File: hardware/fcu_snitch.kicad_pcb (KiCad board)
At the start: 2 copper layers, 105 parts, among them IC1 STM32WLE5CCU6, J1 SMA, J2 02x03_JST_SWD, J3 Conn_02x04_Top_Bottom, J4 Conn_01x02_Socket, J5 Conn_01x04_Socket, Q1 NPN, U1 SKY13373-460LF, U2 BALFHB-WL-02D3, U3 SN74LVC1G3157DBVR, U4 LPS22HBTR, U5 LSM6DSO32, Y1 ABS07L-32.768KHZ-T, Y2 ASTX-H11

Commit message: schematic update and pcb route v1
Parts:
- removed C16: 100p, Capacitor_SMD:C_0402_1005Metric
- removed C47: 100n, Capacitor_SMD:C_0805_2012Metric
- removed C48, C49: 6.8p, Capacitor_SMD:C_0805_2012Metric
- added BT1: Battery_Cell, Battery:BatteryHolder_Keystone_3034_1x20mm, B.Cu at (133.7, 106.5)
- added C8: 100n, Capacitor_SMD:C_0805_2012Metric, B.Cu at (108.8, 97.9)
- added C9: 4.7u, Capacitor_SMD:C_0805_2012Metric, B.Cu at (120.0, 90.4)
- added R27: 100, Resistor_SMD:R_0805_2012Metric, B.Cu at (115.6, 108.8)
- added REF**: MountingHole_2.2mm_M2, MountingHole:MountingHole_2.2mm_M2, F.Cu at (143.1, 75.2)
- added REF**: MountingHole_2.2mm_M2, MountingHole:MountingHole_2.2mm_M2, F.Cu at (143.2, 120.0)
- added REF**: MountingHole_2.2mm_M2, MountingHole:MountingHole_2.2mm_M2, F.Cu at (90.0, 75.4)
- added REF**: MountingHole_2.2mm_M2, MountingHole:MountingHole_2.2mm_M2, F.Cu at (90.0, 120.0)
- C1, C10, C6: value 4.7u -> 100n; moved to B.Cu
- C11: value 100n -> .47u
- C12: value .47u -> 6.8p
- C13, C5: value 100n -> 4.7u; moved to B.Cu
- C14: value .47u -> 100n; footprint Capacitor_SMD:C_0402_1005Metric -> Capacitor_SMD:C_0805_2012Metric; moved to B.Cu
- C15: value 68p -> 6.8p; footprint Capacitor_SMD:C_0402_1005Metric -> Capacitor_SMD:C_0805_2012Metric
- C17: value 8p -> 100n; footprint Capacitor_SMD:C_0402_1005Metric -> Capacitor_SMD:C_0805_2012Metric
- C18: value 0.7p -> 33p; footprint Capacitor_SMD:C_0402_1005Metric -> Capacitor_SMD:C_0805_2012Metric; moved to B.Cu
- C19, C21: value 3p -> C; footprint Capacitor_SMD:C_0402_1005Metric -> Capacitor_SMD:C_0805_2012Metric
- C2, C3, C4, C7, D6, R17, R22, R24: moved to B.Cu
- C20: value 68p -> C; footprint Capacitor_SMD:C_0402_1005Metric -> Capacitor_SMD:C_0805_2012Metric
- C22: value ~ -> 8p; footprint Capacitor_SMD:C_0402_1005Metric -> Capacitor_SMD:C_0805_2012Metric; moved to B.Cu
- C23: value 68p -> 1n; moved to B.Cu
- C24, C27: value ~ -> 10p; moved to B.Cu
- C25: value 68p -> ~; footprint Capacitor_SMD:C_0402_1005Metric -> Capacitor_SMD:C_0805_2012Metric; moved to B.Cu
- C26: value 8p -> 1n; moved to B.Cu
- C28: value 3p -> .47u; moved to B.Cu
- C29: value 8p -> 68p; moved to B.Cu
- C30: value ~ -> 0.7p; footprint Capacitor_SMD:C_0805_2012Metric -> Capacitor_SMD:C_0402_1005Metric
- C31: value 10p -> 39p; footprint Capacitor_SMD:C_0805_2012Metric -> Capacitor_SMD:C_0402_1005Metric
- C32: value 1n -> 2p; footprint Capacitor_SMD:C_0805_2012Metric -> Capacitor_SMD:C_0402_1005Metric
- C33: value 1n -> 33p; footprint Capacitor_SMD:C_0805_2012Metric -> Capacitor_SMD:C_0402_1005Metric
- C34: value 10p -> 100p; footprint Capacitor_SMD:C_0805_2012Metric -> Capacitor_SMD:C_0402_1005Metric
- C35: value C -> 8p; footprint Capacitor_SMD:C_0805_2012Metric -> Capacitor_SMD:C_0402_1005Metric
- C36: value C -> ~; footprint Capacitor_SMD:C_0805_2012Metric -> Capacitor_SMD:C_0402_1005Metric
- C37: value C -> 100p; footprint Capacitor_SMD:C_0805_2012Metric -> Capacitor_SMD:C_0402_1005Metric
- C38, C43: value 100n -> 68p; footprint Capacitor_SMD:C_0805_2012Metric -> Capacitor_SMD:C_0402_1005Metric
- C39, C40, C41: footprint Capacitor_SMD:C_0805_2012Metric -> Capacitor_SMD:C_0402_1005Metric; moved to B.Cu
- C42: value 33p -> 100n; footprint Capacitor_SMD:C_0805_2012Metric -> Capacitor_SMD:C_0402_1005Metric; moved to B.Cu
- C44: value 0.1 -> 8p; footprint Capacitor_SMD:C_0805_2012Metric -> Capacitor_SMD:C_0402_1005Metric
- C45: value 100n -> ~; footprint Capacitor_SMD:C_0805_2012Metric -> Capacitor_SMD:C_0402_1005Metric
- C46: value 100n -> 3p
- D2: value D_Schottky -> ESDS304; footprint Diode_SMD:D_SMA -> Package_TO_SOT_SMD:SOT-23-5
- D3: value ESD8742MUT5G -> ESDS304; footprint imported-footprints:X3DFN2_ONS -> Package_TO_SOT_SMD:SOT-23-5
- D7: value ESDS304 -> D_Schottky; footprint Package_TO_SOT_SMD:SOT-23-5 -> Diode_SMD:D_SMA; moved to B.Cu
- D8: value ESDS304 -> ESD8742MUT5G; footprint Package_TO_SOT_SMD:SOT-23-5 -> imported-footprints:X3DFN2_ONS
- J1: value SMA -> Conn_01x02_Socket; footprint imported-footprints:CINCH_142-0701-231 -> Connector_JST:JST_PH_S2B-PH-K_1x02_P2.00mm_Horizontal
- J2: value 02x03_JST_SWD -> Conn_02x04_Top_Bottom; footprint Connector_PinSocket_1.00mm:PinSocket_2x03_P1.00mm_Vertical_SMD -> Connector_JST:JST_PHD_S8B-PHDSS_2x04_P2.00mm_Horizontal
- J3: value Conn_02x04_Top_Bottom -> Conn_01x04_Socket; footprint Connector_JST:JST_PHD_S8B-PHDSS_2x04_P2.00mm_Horizontal -> Connector_JST:JST_PH_S4B-PH-K_1x04_P2.00mm_Horizontal
- J4: value Conn_01x02_Socket -> 02x03_JST_SWD; footprint Connector_JST:JST_PH_S2B-PH-K_1x02_P2.00mm_Horizontal -> Connector_PinSocket_1.00mm:PinSocket_2x03_P1.00mm_Vertical_SMD
- J5: value Conn_01x04_Socket -> SMA; footprint Connector_JST:JST_PH_S4B-PH-K_1x04_P2.00mm_Horizontal -> Connector_Coaxial:SMA_Amphenol_132289_EdgeMount
- L1: value L -> 15u; footprint imported-footprints:IND_BLM18KG601SN1D_MUR-M -> Inductor_SMD:L_0402_1005Metric
- L2: value 15u -> 600R@100MHz; footprint Inductor_SMD:L_0402_1005Metric -> imported-footprints:IND_BLM18KG601SN1D_MUR-M; moved to B.Cu
- L3: value 47n -> 600R@100MHz; footprint Inductor_SMD:L_0402_1005Metric -> imported-footprints:IND_BLM18KG601SN1D_MUR-M; moved to B.Cu
- L6: value 2.6n -> 47n
- L7: value 10n -> 3.6n
- L8: value 2.6n -> 8.7n
- L9: value L_Ferrite_Small -> 2.6n; footprint imported-footprints:IND_BLM18KG601SN1D_MUR-M -> Inductor_SMD:L_0402_1005Metric
- Q1: footprint Package_TO_SOT_THT:TO-92_Inline -> Package_TO_SOT_SMD:SOT-23; moved to B.Cu
- R1: value 100 -> R
- R12, R16, R19, R20: value R_Small_US -> R
- R26, R3, R4, R5, R6, R7: value R -> R_Small_US
- U1: value SKY13373-460LF -> LSM6DSO32; footprint imported-footprints:SKY13373-460LF_SKY -> imported-footprints:LGA-14L_2P5X3X0P83_STM-L
- U2: value BALFHB-WL-02D3 -> LPS22HBTR; footprint imported-footprints:CSPG8_STM -> imported-footprints:HLGA10_2X2_STM-L
- U3: value SN74LVC1G3157DBVR -> SKY13373-460LF; footprint imported-footprints:DBV6 -> imported-footprints:SKY13373-460LF_SKY
- U4: value LPS22HBTR -> SN74LVC1G3157DBVR; footprint imported-footprints:HLGA10_2X2_STM-L -> imported-footprints:DBV6; moved to B.Cu
- U5: value LSM6DSO32 -> BALFHB-WL-05D3; footprint imported-footprints:LGA-14L_2P5X3X0P83_STM-L -> imported-footprints:BGA8_BALFHB_STM
- moved D1 121.1 mm to (98.5, 82.5), turned to 90 degrees
- moved J2 108.7 mm to (97.0, 105.8), turned to -90 degrees
- moved D5 103.5 mm to (110.4, 110.9)
- moved J3 99.4 mm to (94.5, 93.9), turned to -90 degrees
- moved U4 98.8 mm to (117.4, 96.3), turned to -90 degrees
- moved R23 95.4 mm to (105.1, 88.1), turned to 90 degrees
- moved J1 92.4 mm to (94.4, 81.8), turned to -90 degrees
- moved C45 91.9 mm to (118.0, 114.8), turned to -90 degrees
- moved J4 91.5 mm to (111.1, 107.4), turned to 90 degrees
- moved R16 91.1 mm to (101.8, 110.7), turned to -90 degrees
- moved R15 90.3 mm to (103.1, 96.9), turned to 180 degrees
- moved D4 88.8 mm to (99.0, 98.0), turned to 180 degrees
- moved R12 88.7 mm to (99.8, 110.7), turned to 90 degrees
- moved R5 88.7 mm to (96.2, 120.8), turned to 180 degrees
- moved R14 88.2 mm to (102.3, 99.9), turned to -90 degrees
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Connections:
- C10 pad 1: +3.3V -> VDDA
- C11 pad 1: +3.3V -> GND
- C11 pad 2: GND -> /STM32WLE5 + Radio/VDDRF1V55
- C12 pad 1: /ST-MCU/VDDRF1V55 -> Net-(IC1-PC15-OSC32_OUT)
- C13 pad 1: /ST-MCU/VDDRF1V55 -> +3.3V
- C14 pad 1: /ST-MCU/VR_PA -> +3.3V
- C15 pad 1: /ST-MCU/VR_PA -> Net-(IC1-PC14-OSC32_IN)
- C17 pad 1: Net-(C17-Pad1) -> /STM32WLE5 + Radio/VBAT
- C18 pad 1: Net-(C18-Pad1) -> /STM32WLE5 + Radio/VDDRF1V55
- C19 pad 1: Net-(C17-Pad1) -> Net-(C19-Pad1)
- C19 pad 2: Net-(C18-Pad1) -> Net-(Y2-TRI_STATE)
- C20 pad 1: Net-(C20-Pad1) -> Net-(IC1-OSC_IN)
- C20 pad 2: Net-(C17-Pad1) -> GND
- C21 pad 1: Net-(U1-J2) -> Net-(Y2-TRI_STATE)
- C22 pad 1: Net-(U1-J3) -> +3.3V
- C23 pad 1: Net-(U1-J1) -> Net-(IC1-PA6)
- C23 pad 2: Net-(U2-RFO_OUT) -> GND
- C24 pad 1: Net-(U1-RFC) -> Net-(IC1-PA6)
- C25 pad 1: Net-(U1-RFC) -> +3.3V
- C25 pad 2: Net-(C25-Pad2) -> GND
- C26 pad 1: Net-(D3-A2) -> Net-(IC1-PA7)
- C27 pad 1: Net-(C25-Pad2) -> Net-(IC1-PA7)
- C28 pad 1: /ST-MCU/VDDRF1V55 -> GND
- C28 pad 2: GND -> Net-(IC1-VR_PA)
- C29 pad 1: +3.3V -> GND
- C29 pad 2: GND -> Net-(IC1-VR_PA)
- C3 pad 1: +3.3V -> /NRST
- C30 pad 1: +3.3V -> Net-(C30-Pad1)
- C31 pad 1: Net-(IC1-PA6) -> Net-(U5-RFO_OUT)
- C31 pad 2: GND -> Net-(U3-J3)
- C32 pad 1: Net-(IC1-PA6) -> Net-(C32-Pad1)
- C32 pad 2: GND -> Net-(C30-Pad1)
- C33 pad 1: Net-(IC1-PA7) -> /STM32WLE5 + Radio/VDDRF1V55
- C34 pad 1: Net-(IC1-PA7) -> Net-(U5-RFO_IN)
- C34 pad 2: GND -> Net-(IC1-RFO_LP)
- C35 pad 1: Net-(IC1-OSC_IN) -> Net-(C32-Pad1)
- C36 pad 1: Net-(C36-Pad1) -> Net-(U3-RFC)
- C36 pad 2: Net-(Y2-TRI_STATE) -> GND
- C37 pad 1: Net-(Y2-TRI_STATE) -> GND
- C37 pad 2: GND -> Net-(U3-J2)
- C38 pad 1: /NRST -> Net-(C38-Pad1)
- C38 pad 2: GND -> Net-(C32-Pad1)
- C41 pad 1: /ST-MCU/VDDRF1V55 -> /STM32WLE5 + Radio/VDDPA
- C42 pad 1: /ST-MCU/VDDPA -> /STM32WLE5 + Radio/VDDPA
- C43 pad 1: /ST-MCU/VDDPA -> Net-(U3-RFC)
- C43 pad 2: GND -> Net-(C43-Pad2)
- C44 pad 1: /ST-MCU/VBAT -> Net-(D8-A2)
- C45 pad 1: +3.3V -> Net-(C43-Pad2)
- C46 pad 1: +3.3V -> Net-(U3-J1)
- C5 pad 1: /ST-MCU/VBAT -> +3.3V
- C6 pad 1: VDDA -> +3.3V
- C7 pad 1: VDDA -> +3.3V
- D1 pad 1: Net-(J4-Pin_2) -> Net-(J1-Pin_2)
- D1 pad 2: Net-(J4-Pin_1) -> Net-(J1-Pin_1)
- D2 pad 1: /ST-MCU/VBAT -> Net-(J2-Pin_4)
- D2 pad 2: Net-(D2-A) -> GND
- D3 pad 1: GND -> unconnected-(D3-K-Pad1)
- D3 pad 2: Net-(D3-A2) -> GND
- D4 pad 1: /ST-MCU/SPI2_{CS} -> /STM32WLE5 + Radio/SPI2_{CS}
- D4 pad 3: /ST-MCU/SPI2_{MISO} -> Net-(J3-Pin_2)
- D4 pad 4: Net-(J5-Pin_3) -> Net-(J3-Pin_3)
- D4 pad 5: Net-(J5-Pin_4) -> Net-(J3-Pin_4)
- D6 pad 1: Net-(J3-Pin_4) -> /BOOT0
- D6 pad 3: Net-(J3-Pin_3) -> /SWDIO
- D6 pad 4: Net-(J3-Pin_2) -> /SWCLK
- D7 pad 1: unconnected-(D7-K-Pad1) -> Net-(D7-K)
- D7 pad 2: GND -> +3.3V
- D8 pad 1: /BOOT0 -> GND
- D8 pad 2: unconnected-(D8-A-Pad2) -> Net-(D8-A2)
- IC1 pad 1: /ST-MCU/IMU_{SCK} -> /STM32WLE5 + Radio/IMU_{SCK}
- IC1 pad 10: /ST-MCU/RX_{USART2} -> /STM32WLE5 + Radio/RX_{USART2}
- IC1 pad 12: /ST-MCU/CK_{USART2} -> /STM32WLE5 + Radio/CK_{USART2}
- IC1 pad 13: /ST-MCU/SPI2_{MISO} -> /STM32WLE5 + Radio/SPI2_{MISO}
- IC1 pad 16: /ST-MCU/SPI2_{SCK} -> /STM32WLE5 + Radio/SPI2_{SCK}
- IC1 pad 17: /ST-MCU/SELECTPWR -> /STM32WLE5 + Radio/SELECTPWR
- IC1 pad 2: /ST-MCU/IMU_{MISO} -> /STM32WLE5 + Radio/IMU_{MISO}
- IC1 pad 20: Net-(IC1-RFI_P) -> /STM32WLE5 + Radio/RFI_P
- IC1 pad 21: Net-(IC1-RFI_N) -> /STM32WLE5 + Radio/RFI_N
- IC1 pad 22: /ST-MCU/RFO_LP -> Net-(IC1-RFO_LP)
- IC1 pad 24: /ST-MCU/VR_PA -> Net-(IC1-VR_PA)
- IC1 pad 25: /ST-MCU/VDDPA -> /STM32WLE5 + Radio/VDDPA
- IC1 pad 29: /ST-MCU/VDDRF1V55 -> /STM32WLE5 + Radio/VDDRF1V55
- IC1 pad 3: /ST-MCU/IMU_{MOSI} -> /STM32WLE5 + Radio/IMU_{MOSI}
- IC1 pad 31: /ST-MCU/BUZZ_OUT -> /STM32WLE5 + Radio/BUZZ_OUT
- IC1 pad 32: /ST-MCU/IMU_{INT} -> /STM32WLE5 + Radio/IMU_{INT}
- IC1 pad 33: /ST-MCU/SPI2_{MOSI} -> /STM32WLE5 + Radio/SPI2_{MOSI}
- IC1 pad 34: /ST-MCU/VMONITOR -> /VMON
- IC1 pad 35: /ST-MCU/SPI2_{CS} -> /STM32WLE5 + Radio/SPI2_{CS}
- IC1 pad 37: /ST-MCU/VBAT -> /STM32WLE5 + Radio/VBAT
- IC1 pad 4: /ST-MCU/TX -> /STM32WLE5 + Radio/TX
- IC1 pad 45: /ST-MCU/VDDRF1V55 -> /STM32WLE5 + Radio/VDDRF1V55
- IC1 pad 47: /ST-MCU/VLXSMPS -> /STM32WLE5 + Radio/VLXSMPS
- IC1 pad 5: /ST-MCU/RX -> /STM32WLE5 + Radio/RX
- IC1 pad 6: /ST-MCU/IMU_{CS} -> /STM32WLE5 + Radio/IMU_{CS}
- IC1 pad 7: /ST-MCU/CTS_{USART2} -> /STM32WLE5 + Radio/CTS_{USART2}
- IC1 pad 8: /ST-MCU/RTS_{USART2} -> /STM32WLE5 + Radio/RTS_{USART2}
- IC1 pad 9: /ST-MCU/TX_{USART2} -> /STM32WLE5 + Radio/TX_{USART2}
- J1 pad 1: Net-(D3-A2) -> Net-(J1-Pin_1)
- J2 pad 2: /NRST -> /RX1
- J2 pad 3: /BOOT0 -> /TX1
- J2 pad 4: GND -> Net-(J2-Pin_4)
- J2 pad 5: /SWCLK -> GND
- J2 pad 6: /SWDIO -> /CTS
- J3 pad 1: +3.3V -> /STM32WLE5 + Radio/SPI2_{CS}
- J4 pad 1: Net-(J4-Pin_1) -> +3.3V
- J4 pad 2: Net-(J4-Pin_2) -> /NRST
- J5 pad 1: /ST-MCU/SPI2_{CS} -> Net-(D8-A2)
- J5 pad 2: Net-(J5-Pin_2) -> GND
- L1 pad 1: Net-(D2-A) -> /STM32WLE5 + Radio/VLXSMPS
- L1 pad 2: VDDA -> /STM32WLE5 + Radio/VDDRF1V55
- L2 pad 1: /ST-MCU/VLXSMPS -> +3.3V
- L2 pad 2: /ST-MCU/VDDRF1V55 -> VDDA
- L3 pad 1: Net-(IC1-RFO_HP) -> Net-(IC1-PB0-VDD_TCXO)
- L3 pad 2: /ST-MCU/VR_PA -> Net-(Y2-VDD)
- L4 pad 1: Net-(C18-Pad1) -> Net-(IC1-VR_PA)
- L4 pad 2: /ST-MCU/VR_PA -> Net-(IC1-RFO_LP)
- L5 pad 1: Net-(C18-Pad1) -> Net-(IC1-RFO_HP)
- L5 pad 2: /ST-MCU/RFO_LP -> Net-(C30-Pad1)
- L6 pad 1: Net-(C17-Pad1) -> Net-(IC1-VR_PA)
- L6 pad 2: Net-(C18-Pad1) -> Net-(C30-Pad1)
- L7 pad 1: Net-(U1-J2) -> Net-(C32-Pad1)
- L7 pad 2: Net-(C20-Pad1) -> Net-(C30-Pad1)
- L8 pad 1: Net-(D3-A2) -> Net-(U3-J1)
- L8 pad 2: Net-(C25-Pad2) -> Net-(C38-Pad1)
- L9 pad 1: Net-(IC1-PB0-VDD_TCXO) -> Net-(D8-A2)
- L9 pad 2: Net-(Y2-VDD) -> Net-(C43-Pad2)
- Q1 pad 1: GND -> Net-(Q1-B)
- Q1 pad 2: Net-(Q1-B) -> GND
- R1 pad 1: +3.3V -> /STM32WLE5 + Radio/IMU_{CS}
- R1 pad 2: Net-(U1-VDD) -> +3.3V
- R10 pad 1: /ST-MCU/CTS_{USART2} -> /STM32WLE5 + Radio/RX_{USART2}
- R10 pad 2: Net-(J3-Pin_6) -> /RX1
- R11 pad 1: /ST-MCU/RTS_{USART2} -> /STM32WLE5 + Radio/TX_{USART2}
- R11 pad 2: Net-(J3-Pin_7) -> /TX1
- R12 pad 1: /ST-MCU/CK_{USART2} -> /VMON
- R12 pad 2: Net-(J3-Pin_8) -> Net-(J2-Pin_4)
- R13 pad 1: /ST-MCU/RX_{USART2} -> /STM32WLE5 + Radio/SPI2_{CS}
- R13 pad 2: Net-(J3-Pin_2) -> +3.3V
- R14 pad 1: /ST-MCU/TX_{USART2} -> /STM32WLE5 + Radio/SPI2_{CS}
- R14 pad 2: Net-(J3-Pin_3) -> GND
- R15 pad 1: /ST-MCU/SPI2_{MISO} -> /STM32WLE5 + Radio/SPI2_{MISO}
- R15 pad 2: Net-(J5-Pin_2) -> Net-(J3-Pin_2)
- R16 pad 1: /ST-MCU/SPI2_{MOSI} -> GND
- R16 pad 2: Net-(J5-Pin_3) -> /VMON
- R17 pad 1: /ST-MCU/SPI2_{SCK} -> /STM32WLE5 + Radio/SPI2_{MOSI}
- R17 pad 2: Net-(J5-Pin_4) -> Net-(J3-Pin_3)
- R18 pad 1: Net-(U5-SCL) -> /STM32WLE5 + Radio/SPI2_{SCK}
- R18 pad 2: /ST-MCU/IMU_{SCK} -> Net-(J3-Pin_4)
- R19 pad 1: Net-(U5-SDA) -> +3.3V
- R19 pad 2: /ST-MCU/IMU_{MOSI} -> Net-(BZ1-+)
- R2 pad 1: Net-(IC1-OSC_OUT) -> /STM32WLE5 + Radio/TX
- R2 pad 2: Net-(C36-Pad1) -> Net-(J1-Pin_1)
- R20 pad 1: Net-(U5-SDO/SA0) -> GND
- R20 pad 2: /ST-MCU/IMU_{MISO} -> Net-(BZ1-+)
- R21 pad 1: +3.3V -> /HSCL
- R21 pad 2: Net-(BZ1-+) -> +3.3V
- R22 pad 1: /ST-MCU/IMU_{CS} -> /STM32WLE5 + Radio/BUZZ_OUT
- R22 pad 2: +3.3V -> Net-(Q1-B)
- R23 pad 1: +3.3V -> /HSDA
- R23 pad 2: Net-(U4-CS) -> +3.3V
- R24 pad 1: /HSDA -> /BOOT0
- R24 pad 2: +3.3V -> GND
- R25 pad 1: /HSCL -> Net-(D7-K)
- R25 pad 2: +3.3V -> /STM32WLE5 + Radio/VBAT
- R26 pad 1: GND -> Net-(IC1-OSC_OUT)
- R26 pad 2: Net-(BZ1-+) -> Net-(C19-Pad1)
- R3 pad 1: /BOOT0 -> Net-(U1-SCL)
- R3 pad 2: GND -> /STM32WLE5 + Radio/IMU_{SCK}
- R4 pad 1: +3.3V -> /STM32WLE5 + Radio/RX
- R4 pad 2: Net-(D2-A) -> Net-(J1-Pin_2)
- R5 pad 1: GND -> /STM32WLE5 + Radio/CTS_{USART2}
- R5 pad 2: /ST-MCU/VMONITOR -> /CTS
- R6 pad 1: /ST-MCU/BUZZ_OUT -> /STM32WLE5 + Radio/RTS_{USART2}
- R6 pad 2: Net-(Q1-B) -> /RTS
- R7 pad 1: /ST-MCU/VMONITOR -> /STM32WLE5 + Radio/CK_{USART2}
- R7 pad 2: Net-(J3-Pin_4) -> /CK
- R8 pad 1: /ST-MCU/RX -> Net-(U1-SDA)
- R8 pad 2: Net-(J4-Pin_2) -> /STM32WLE5 + Radio/IMU_{MOSI}
- R9 pad 1: /ST-MCU/TX -> Net-(U1-SDO/SA0)
- R9 pad 2: Net-(J4-Pin_1) -> /STM32WLE5 + Radio/IMU_{MISO}
- U1 pad 1: Net-(U1-J1) -> Net-(U1-SDO/SA0)
- U1 pad 10: GND -> unconnected-(U1-NC-Pad10)
- U1 pad 11: Net-(U1-RFC) -> unconnected-(U1-NC-Pad11)
- U1 pad 12: GND -> /STM32WLE5 + Radio/IMU_{CS}
- U1 pad 13: GND -> Net-(U1-SCL)
- U1 pad 2: GND -> /HSDA
- U1 pad 3: Net-(U1-J3) -> /HSCL
- U1 pad 4: Net-(IC1-PA6) -> /STM32WLE5 + Radio/IMU_{INT}
- U1 pad 5: Net-(IC1-PA7) -> +3.3V
- U1 pad 6: Net-(U1-VDD) -> GND
- U1 pad 8: GND -> +3.3V
- U1 pad 9: Net-(U1-J2) -> /DRDY
- U3 pad 1: /ST-MCU/VDDRF1V55 -> Net-(U3-J1)
- U3 pad 3: +3.3V -> Net-(U3-J3)
- U3 pad 4: /ST-MCU/VDDPA -> Net-(IC1-PA6)
- U3 pad 5: +3.3V -> Net-(IC1-PA7)
- U3 pad 6: /ST-MCU/SELECTPWR -> Net-(U3-VDD)
- U4 pad 1: +3.3V -> /STM32WLE5 + Radio/VDDRF1V55
- U4 pad 2: /HSCL -> GND
- U4 pad 3: GND -> +3.3V
- U4 pad 4: /HSDA -> /STM32WLE5 + Radio/VDDPA
- U4 pad 5: GND -> +3.3V
- U4 pad 6: Net-(U4-CS) -> /STM32WLE5 + Radio/SELECTPWR
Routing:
- net /STM32WLE5 + Radio/CTS_{USART2}: track 0.00 -> 34.7 mm, vias 0 -> 2
- net /VMON: track 0.00 -> 31.9 mm, vias 0 -> 2
- net /STM32WLE5 + Radio/SPI2_{CS}: track 0.00 -> 30.5 mm, vias 0 -> 4
- net /SWCLK: track 0.00 -> 30.4 mm, vias 0 -> 3
- net /STM32WLE5 + Radio/RTS_{USART2}: track 0.00 -> 28.2 mm, vias 0 -> 2
- net Net-(J3-Pin_3): track 0.00 -> 23.9 mm, vias 0 -> 2
- net /STM32WLE5 + Radio/CK_{USART2}: track 0.00 -> 22.2 mm, vias 0 -> 2
- net /STM32WLE5 + Radio/RX: track 0.00 -> 21.1 mm
- net /SWDIO: track 0.00 -> 21.0 mm, vias 0 -> 4
- net Net-(J3-Pin_4): track 0.00 -> 20.5 mm, vias 0 -> 2
- net /STM32WLE5 + Radio/IMU_{INT}: track 0.00 -> 20.3 mm, vias 0 -> 4
- net /STM32WLE5 + Radio/VBAT: track 0.00 -> 19.2 mm, vias 0 -> 1
- net /STM32WLE5 + Radio/TX: track 0.00 -> 17.5 mm, vias 0 -> 2
- net /NRST: track 0.00 -> 17.3 mm, vias 0 -> 1
- net /BOOT0: track 0.00 -> 15.9 mm, vias 0 -> 3
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- added copper zone on In2.Cu, net /STM32WLE5 + Radio/VDDPA
- added copper zone on In2.Cu, net Net-(IC1-VR_PA)
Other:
- board outline added: 57.8 x 50.1 mm
- copper layers 2 -> 6

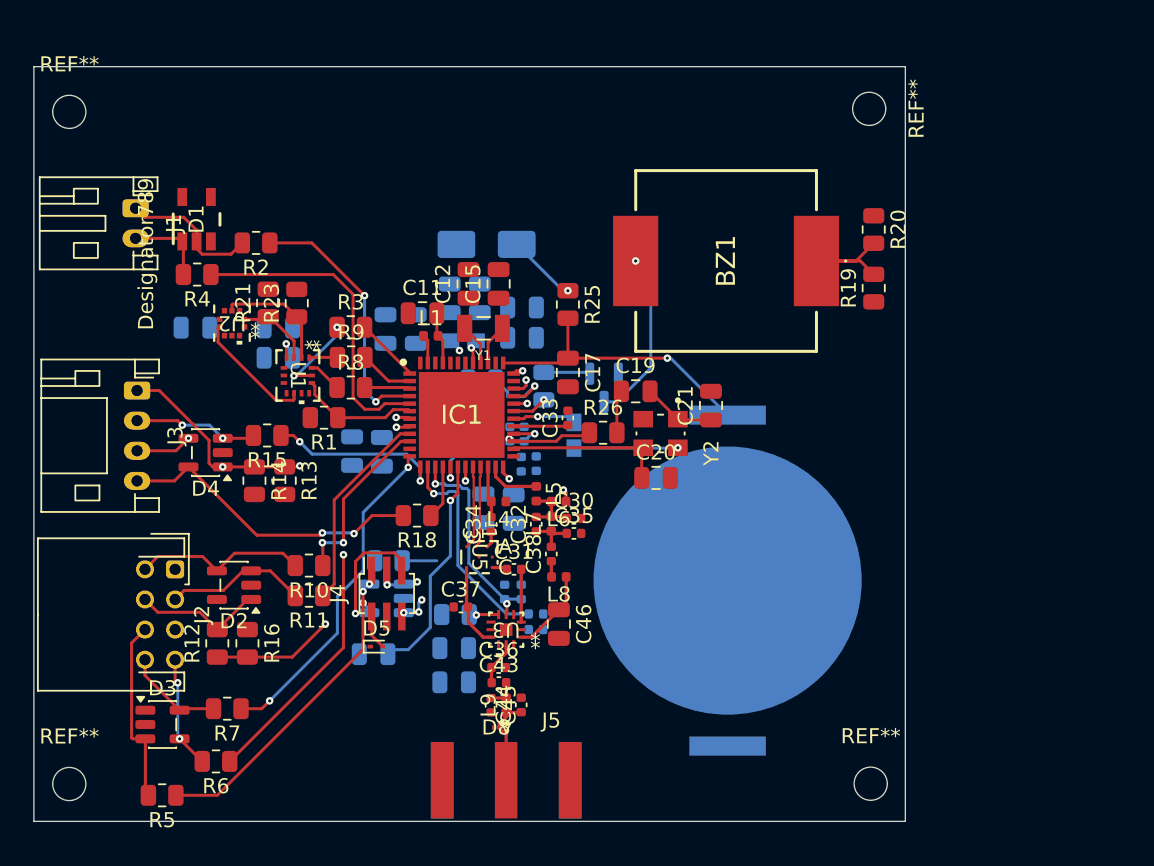
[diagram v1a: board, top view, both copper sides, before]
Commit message: better pcb route (no test pads)
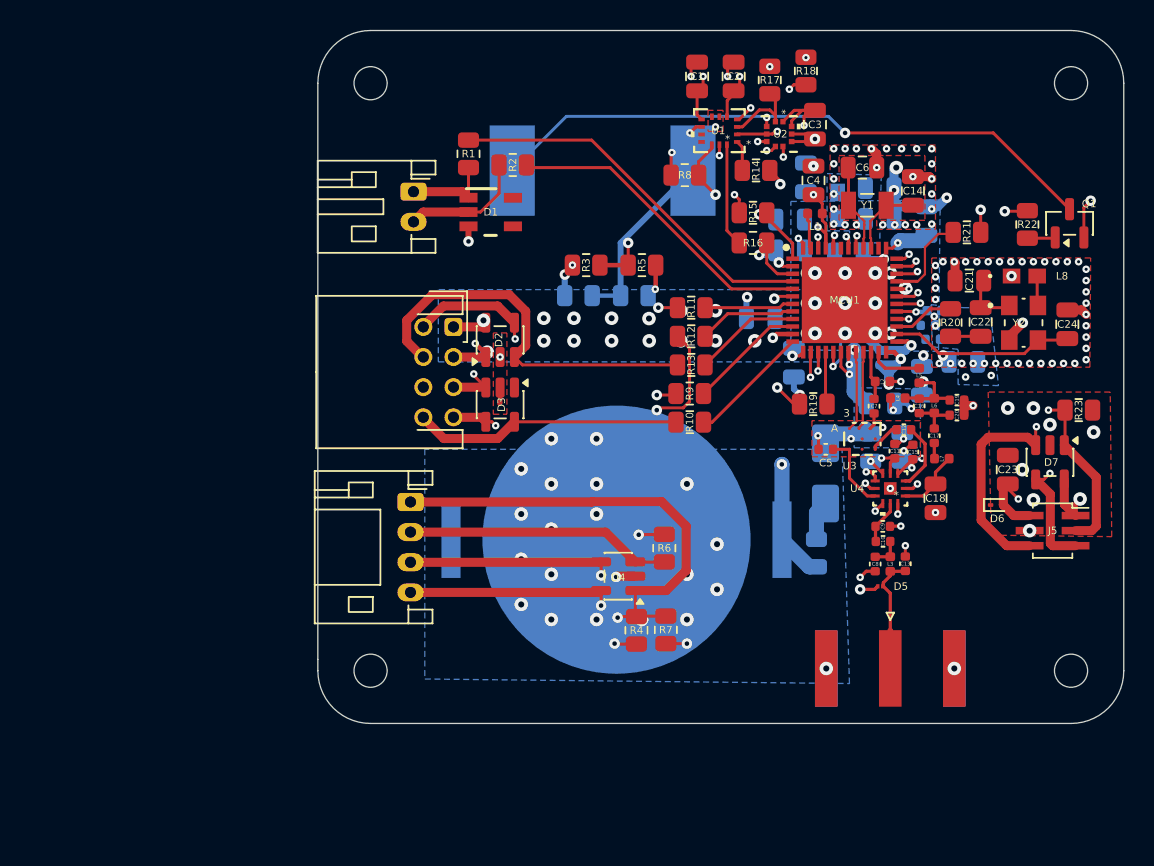
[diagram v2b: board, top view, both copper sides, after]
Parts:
- removed the C10 at (120.0, 88.4)
- removed the C12 at (116.5, 86.8)
- removed the C13 at (113.0, 89.8)
- removed the C17 at (123.1, 92.7)
- removed the C18 at (114.0, 94.3)
- removed the C19 at (127.6, 94.0)
- removed the C20 at (128.9, 99.7)
- removed the C7 at (115.2, 87.8)
- removed the C8 at (108.8, 97.9)
- removed the C9 at (120.0, 90.4)
- removed the D5 at (110.4, 110.9)
- removed the J4 at (111.1, 107.4)
- removed the L2 at (116.1, 90.6)
- removed the L3 at (123.5, 96.9)
- removed REF** (x4): MountingHole_2.2mm_M2, MountingHole:MountingHole_2.2mm_M2
- removed the U4 at (117.4, 96.3)
- added C30: 68p, Capacitor_SMD:C_0805_2012Metric, B.Cu at (146.6, 93.2)
- added C31: 8p, Capacitor_SMD:C_0805_2012Metric, B.Cu at (145.3, 97.7)
- added C32: 100n, Capacitor_SMD:C_0402_1005Metric, B.Cu at (144.9, 91.7)
- added C34: 4.7u, Capacitor_SMD:C_0805_2012Metric, B.Cu at (143.8, 82.5)
- added C35: 33p, Capacitor_SMD:C_0402_1005Metric, B.Cu at (143.8, 91.7)
- added C36: ~, Capacitor_SMD:C_0805_2012Metric, B.Cu at (143.8, 94.8)
- added C38: 33p, Capacitor_SMD:C_0805_2012Metric, B.Cu at (138.9, 79.8)
- added D8: D_Schottky, Diode_SMD:D_SMA, B.Cu at (140.2, 99.4)
- added H3: MountingHole, MountingHole:MountingHole_2.2mm_M2, F.Cu at (110.0, 73.5)
- added H3: MountingHole, MountingHole:MountingHole_2.2mm_M2, F.Cu at (156.5, 112.5)
- added H3: MountingHole, MountingHole:MountingHole_2.2mm_M2, F.Cu at (156.5, 73.5)
- added H3: MountingHole, MountingHole:MountingHole_2.2mm_M2, F.Cu at (110.0, 112.5)
- added J5: 02x03_SMD, Connector_PinSocket_1.00mm:PinSocket_2x03_P1.00mm_Vertical_SMD, F.Cu at (155.3, 103.2)
- added L8: 600R@100MHz, imported-footprints:IND_BLM18KG601SN1D_MUR-M, F.Cu at (153.4, 86.3)
- added L9: 600R@100MHz, imported-footprints:IND_BLM18KG601SN1D_MUR-M, B.Cu at (141.0, 81.6)
- added U5: SN74LVC1G3157DBVR, imported-footprints:DBV6, B.Cu at (142.1, 88.6)
- BZ1, R25: moved to B.Cu
- C1, C2, C3, Q1, R22: moved to F.Cu
- C11: value .47u -> 100p; footprint Capacitor_SMD:C_0805_2012Metric -> Capacitor_SMD:C_0402_1005Metric
- C14, C6: value 100n -> 6.8p; moved to F.Cu
- C15: value 6.8p -> 100p; footprint Capacitor_SMD:C_0805_2012Metric -> Capacitor_SMD:C_0402_1005Metric
- C22: value 8p -> C; moved to F.Cu
- C23: value 1n -> 100n; footprint Capacitor_SMD:C_0402_1005Metric -> Capacitor_SMD:C_0805_2012Metric; moved to F.Cu
- C24: value 10p -> C; footprint Capacitor_SMD:C_0402_1005Metric -> Capacitor_SMD:C_0805_2012Metric; moved to F.Cu
- C25: value ~ -> .47u
- C26: value 1n -> 33p
- C27: value 10p -> 100n
- C28: value .47u -> 100n
- C29: value 68p -> 100n; footprint Capacitor_SMD:C_0805_2012Metric -> Capacitor_SMD:C_0402_1005Metric
- C33: value 33p -> 100n; footprint Capacitor_SMD:C_0402_1005Metric -> Capacitor_SMD:C_0805_2012Metric; moved to B.Cu
- C37: value 100p -> 100n; footprint Capacitor_SMD:C_0402_1005Metric -> Capacitor_SMD:C_0805_2012Metric; moved to B.Cu
- C39, C42: value 100n -> 4.7u; footprint Capacitor_SMD:C_0402_1005Metric -> Capacitor_SMD:C_0805_2012Metric
- C4: value 100n -> .47u; moved to F.Cu
- C40: footprint Capacitor_SMD:C_0402_1005Metric -> Capacitor_SMD:C_0805_2012Metric
- C41: value 33p -> 100n; footprint Capacitor_SMD:C_0402_1005Metric -> Capacitor_SMD:C_0805_2012Metric
- C5: value 4.7u -> 100p; footprint Capacitor_SMD:C_0805_2012Metric -> Capacitor_SMD:C_0402_1005Metric; moved to F.Cu
- D6: value ESDS304 -> ESD9B3.3ST5G; footprint Package_TO_SOT_SMD:SOT-23-5 -> Diode_SMD:D_SOD-923; moved to F.Cu
- D7: value D_Schottky -> ESDS304; footprint Diode_SMD:D_SMA -> Package_TO_SOT_SMD:SOT-23-5; moved to F.Cu
- J1: value Conn_01x02_Socket -> Conn_01x04_Socket; footprint Connector_JST:JST_PH_S2B-PH-K_1x02_P2.00mm_Horizontal -> Connector_JST:JST_PH_S4B-PH-K_1x04_P2.00mm_Horizontal
- J2: value Conn_02x04_Top_Bottom -> Conn_01x02_Socket; footprint Connector_JST:JST_PHD_S8B-PHDSS_2x04_P2.00mm_Horizontal -> Connector_JST:JST_PH_S2B-PH-K_1x02_P2.00mm_Horizontal
- J3: value Conn_01x04_Socket -> Conn_02x04_Top_Bottom; footprint Connector_JST:JST_PH_S4B-PH-K_1x04_P2.00mm_Horizontal -> Connector_JST:JST_PHD_S8B-PHDSS_2x04_P2.00mm_Horizontal
- R1, R12, R16, R19, R20, R21: value R -> R_Small_US
- R17: value R_Small_US -> R; moved to F.Cu
- R18, R3, R5, R8: value R_Small_US -> R
- R24: value R -> 100
- R26: value R_Small_US -> R; moved to B.Cu
- R27: value 100 -> R
- moved R23 52.4 mm to (157.0, 95.2), turned to 0 degrees
- moved R5 47.5 mm to (128.0, 85.6)
- moved R21 46.6 mm to (149.6, 83.4), turned to 0 degrees
- moved C3 45.8 mm to (139.5, 76.2), turned to -90 degrees
- moved R16 42.8 mm to (135.4, 84.1), turned to 0 degrees
- moved C4 42.2 mm to (139.4, 80.0), turned to -90 degrees
- moved C22 41.1 mm to (150.5, 89.3), turned to 90 degrees
- moved D6 41.0 mm to (151.6, 101.5), turned to 0 degrees
- moved C24 40.2 mm to (156.2, 89.5), turned to 90 degrees
- moved D7 40.1 mm to (155.1, 98.7), turned to -90 degrees
- moved C25 39.9 mm to (149.3, 92.0), turned to 180 degrees
- moved R18 39.2 mm to (138.9, 72.7), turned to 90 degrees
- moved R14 39.2 mm to (135.6, 79.3), turned to 0 degrees
- moved U2 38.4 mm to (137.1, 76.9), turned to -90 degrees
- moved R4 37.5 mm to (127.6, 109.8), turned to -90 degrees
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- renumbered C43 to C10, C31 to C12, C44 to C13, C32 to C16, C38 to C17, C46 to C18, C30 to C19, C35 to C20, C34 to C7, C45 to C8, C36 to C9, D8 to D5, J5 to J4, L4 to L2, L9 to L3, L6 to L4, L7 to L6, L8 to L7, IC1 to MCU1, U5 to U3, U3 to U4
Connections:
- net /STM32WLE5 + Radio/IMU_{INT} renamed /IMU_INT
- C11 pad 1: GND -> Net-(MCU1-PA6)
- C11 pad 2: /STM32WLE5 + Radio/VDDRF1V55 -> GND
- C14 pad 1: +3.3V -> /STM32WLE5 + Radio/OSC_K-
- C14 pad 2: GND -> GND1
- C15 pad 1: Net-(IC1-PC14-OSC32_IN) -> Net-(MCU1-PA7)
- C21 pad 2: GND -> GND1
- C22 pad 1: +3.3V -> Net-(C17-Pad1)
- C22 pad 2: GND -> Net-(Y2-TRI_STATE)
- C23 pad 1: Net-(IC1-PA6) -> /NRST
- C24 pad 1: Net-(IC1-PA6) -> Net-(MCU1-OSC_IN)
- C24 pad 2: GND -> GND1
- C25 pad 1: +3.3V -> GND
- C25 pad 2: GND -> Net-(MCU1-VR_PA)
- C26 pad 1: Net-(IC1-PA7) -> /STM32WLE5 + Radio/VDDRF1V55
- C27 pad 1: Net-(IC1-PA7) -> +3.3V
- C28 pad 1: GND -> /STM32WLE5 + Radio/VBAT
- C28 pad 2: Net-(IC1-VR_PA) -> GND
- C29 pad 1: GND -> +3.3V
- C29 pad 2: Net-(IC1-VR_PA) -> GND
- C3 pad 1: /NRST -> +3.3V
- C33 pad 1: /STM32WLE5 + Radio/VDDRF1V55 -> VDDA
- C37 pad 1: GND -> +3.3V
- C37 pad 2: Net-(U3-J2) -> GND
- C4 pad 1: +3.3V -> GND
- C4 pad 2: GND -> /STM32WLE5 + Radio/VDDRF1V55
- C41 pad 1: /STM32WLE5 + Radio/VDDPA -> +3.3V
- C42 pad 1: /STM32WLE5 + Radio/VDDPA -> +3.3V
- C5 pad 1: +3.3V -> GND
- C5 pad 2: GND -> Net-(U3-J2)
- C6 pad 1: +3.3V -> /STM32WLE5 + Radio/OSC_K+
- C6 pad 2: GND -> GND1
- D1 pad 1: Net-(J1-Pin_2) -> /TX2
- D1 pad 2: Net-(J1-Pin_1) -> /RX2
- D2 pad 1: Net-(J2-Pin_4) -> Net-(J2-Pin_3)
- D4 pad 1: /STM32WLE5 + Radio/SPI2_{CS} -> /SPI2CS
- D4 pad 3: Net-(J3-Pin_2) -> /SPI2MISO
- D4 pad 4: Net-(J3-Pin_3) -> /SPI2MOSI
- D4 pad 5: Net-(J3-Pin_4) -> /SPI2SCK
- D6 pad 1: /BOOT0 -> GND
- D6 pad 2: GND -> /NRST
- D7 pad 1: Net-(D7-K) -> /BOOT0
- D7 pad 2: +3.3V -> GND
- J1 pad 1: Net-(J1-Pin_1) -> /SPI2CS
- J1 pad 2: Net-(J1-Pin_2) -> /SPI2MISO
- J2 pad 1: +3.3V -> /TX2
- J2 pad 2: /RX1 -> /RX2
- J3 pad 1: /STM32WLE5 + Radio/SPI2_{CS} -> +3.3V
- J3 pad 2: Net-(J3-Pin_2) -> /RX1
- J3 pad 3: Net-(J3-Pin_3) -> Net-(J2-Pin_3)
- J3 pad 4: Net-(J3-Pin_4) -> /TX1
- L2 pad 1: Net-(IC1-VR_PA) -> Net-(MCU1-VR_PA)
- L4 pad 1: Net-(IC1-VR_PA) -> Net-(MCU1-VR_PA)
- MCU1 pad 14: Net-(IC1-PA6) -> Net-(MCU1-PA6)
- MCU1 pad 15: Net-(IC1-PA7) -> Net-(MCU1-PA7)
- MCU1 pad 24: Net-(IC1-VR_PA) -> Net-(MCU1-VR_PA)
- MCU1 pad 26: Net-(IC1-OSC_IN) -> Net-(MCU1-OSC_IN)
- MCU1 pad 27: Net-(IC1-OSC_OUT) -> Net-(MCU1-OSC_OUT)
- MCU1 pad 35: /STM32WLE5 + Radio/SPI2_{CS} -> /SPI2CS
- MCU1 pad 39: Net-(IC1-PC14-OSC32_IN) -> /STM32WLE5 + Radio/OSC_K-
- MCU1 pad 40: Net-(IC1-PC15-OSC32_OUT) -> /STM32WLE5 + Radio/OSC_K+
- MCU1 pad 6: /STM32WLE5 + Radio/IMU_{CS} -> /IMU_CS
- R1 pad 1: /STM32WLE5 + Radio/IMU_{CS} -> /STM32WLE5 + Radio/TX
- R1 pad 2: +3.3V -> /TX2
- R10 pad 1: /STM32WLE5 + Radio/RX_{USART2} -> /STM32WLE5 + Radio/CK_{USART2}
- R10 pad 2: /RX1 -> /CK
- R11 pad 1: /STM32WLE5 + Radio/TX_{USART2} -> /STM32WLE5 + Radio/CTS_{USART2}
- R11 pad 2: /TX1 -> /CTS
- R12 pad 1: /VMON -> /STM32WLE5 + Radio/RTS_{USART2}
- R12 pad 2: Net-(J2-Pin_4) -> /RTS
- R13 pad 1: /STM32WLE5 + Radio/SPI2_{CS} -> /STM32WLE5 + Radio/TX_{USART2}
- R13 pad 2: +3.3V -> /TX1
- R14 pad 1: /STM32WLE5 + Radio/SPI2_{CS} -> /IMU_MISO
- R14 pad 2: GND -> /STM32WLE5 + Radio/IMU_{MISO}
- R15 pad 1: /STM32WLE5 + Radio/SPI2_{MISO} -> /IMU_SCK
- R15 pad 2: Net-(J3-Pin_2) -> /STM32WLE5 + Radio/IMU_{SCK}
- R16 pad 1: GND -> /IMU_MOSI
- R16 pad 2: /VMON -> /STM32WLE5 + Radio/IMU_{MOSI}
- R17 pad 1: /STM32WLE5 + Radio/SPI2_{MOSI} -> /HSCL
- R17 pad 2: Net-(J3-Pin_3) -> +3.3V
- R18 pad 1: /STM32WLE5 + Radio/SPI2_{SCK} -> /HSDA
- R18 pad 2: Net-(J3-Pin_4) -> +3.3V
- R19 pad 1: +3.3V -> /STM32WLE5 + Radio/SPI2_{SCK}
- R19 pad 2: Net-(BZ1-+) -> /SPI2SCK
- R2 pad 1: /STM32WLE5 + Radio/TX -> /STM32WLE5 + Radio/RX
- R2 pad 2: Net-(J1-Pin_1) -> /RX2
- R20 pad 1: GND -> Net-(MCU1-OSC_OUT)
- R20 pad 2: Net-(BZ1-+) -> Net-(C17-Pad1)
- R21 pad 1: /HSCL -> /STM32WLE5 + Radio/SPI2_{MOSI}
- R21 pad 2: +3.3V -> /SPI2MOSI
- R23 pad 1: /HSDA -> /BOOT0
- R23 pad 2: +3.3V -> GND
- R24 pad 1: /BOOT0 -> +3.3V
- R24 pad 2: GND -> Net-(U3-VDD)
- R26 pad 1: Net-(IC1-OSC_OUT) -> +3.3V
- R26 pad 2: Net-(C19-Pad1) -> Net-(BZ1-+)
- R27 pad 1: +3.3V -> GND
- R27 pad 2: Net-(U3-VDD) -> Net-(BZ1-+)
- R3 pad 1: Net-(U1-SCL) -> /VMON
- R3 pad 2: /STM32WLE5 + Radio/IMU_{SCK} -> Net-(J2-Pin_3)
- R4 pad 1: /STM32WLE5 + Radio/RX -> /SPI2CS
- R4 pad 2: Net-(J1-Pin_2) -> GND
- R5 pad 1: /STM32WLE5 + Radio/CTS_{USART2} -> GND
- R5 pad 2: /CTS -> /VMON
- R6 pad 1: /STM32WLE5 + Radio/RTS_{USART2} -> /STM32WLE5 + Radio/SPI2_{MISO}
- R6 pad 2: /RTS -> /SPI2MISO
- R7 pad 1: /STM32WLE5 + Radio/CK_{USART2} -> /SPI2CS
- R7 pad 2: /CK -> +3.3V
- R8 pad 1: Net-(U1-SDA) -> /IMU_CS
- R8 pad 2: /STM32WLE5 + Radio/IMU_{MOSI} -> +3.3V
- R9 pad 1: Net-(U1-SDO/SA0) -> /STM32WLE5 + Radio/RX_{USART2}
- R9 pad 2: /STM32WLE5 + Radio/IMU_{MISO} -> /RX1
- U1 pad 1: Net-(U1-SDO/SA0) -> /IMU_MISO
- U1 pad 12: /STM32WLE5 + Radio/IMU_{CS} -> /IMU_CS
- U1 pad 13: Net-(U1-SCL) -> /IMU_SCK
- U1 pad 14: Net-(U1-SDA) -> /IMU_MOSI
- U4 pad 4: Net-(IC1-PA6) -> Net-(MCU1-PA7)
- U4 pad 5: Net-(IC1-PA7) -> Net-(MCU1-PA6)
- Y1 pad 1: Net-(IC1-PC14-OSC32_IN) -> /STM32WLE5 + Radio/OSC_K-
- Y1 pad 2: Net-(IC1-PC15-OSC32_OUT) -> /STM32WLE5 + Radio/OSC_K+
- Y2 pad 2: GND -> GND1
- Y2 pad 3: Net-(IC1-OSC_IN) -> Net-(MCU1-OSC_IN)
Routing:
- net /SPI2CS: track 0.00 -> 64.2 mm, vias 0 -> 2
- net /SPI2MOSI: track 0.00 -> 52.1 mm, vias 0 -> 2
- net GND: track 0.00 -> 51.5 mm, vias 0 -> 85
- net /SPI2SCK: track 0.00 -> 35.0 mm, vias 0 -> 2
- net /STM32WLE5 + Radio/SPI2_{CS}: track 30.5 -> 0.00 mm, vias 4 -> 0
- net Net-(BZ1--): track 11.5 -> 41.0 mm
- net /STM32WLE5 + Radio/CTS_{USART2}: track 34.7 -> 5.92 mm, vias 2 -> 0
- net +3.3V: track 6.68 -> 33.0 mm, vias 4 -> 36
- net Net-(J3-Pin_3): track 23.9 -> 0.00 mm, vias 2 -> 0
- net /STM32WLE5 + Radio/RTS_{USART2}: track 28.2 -> 6.50 mm, vias 2 -> 0
- net Net-(J3-Pin_4): track 20.5 -> 0.00 mm, vias 2 -> 0
- net /SPI2MISO: track 0.00 -> 18.0 mm
- net /TX1: track 9.45 -> 26.6 mm
- net /STM32WLE5 + Radio/VBAT: track 19.2 -> 34.9 mm, vias 1 -> 2
- net Net-(IC1-PA6): track 14.4 -> 0.00 mm, vias 1 -> 0
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- added copper zone on B.Cu, net +3.3V
- added copper zone on In3.Cu, net +3.3V
- added copper zone on B.Cu, net /STM32WLE5 + Radio/VBAT
- added copper zone on In3.Cu, net /STM32WLE5 + Radio/VDDRF1V55
- added copper zone on B.Cu, net GND
- added copper zone on F.Cu, net GND
- added copper zone on In1.Cu, net GND
- added copper zone on F.Cu, net GND1
- added copper zone on In1.Cu, net GND1
- added copper zone on In3.Cu, net Net-(MCU1-VR_PA)
- added copper zone on B.Cu, net VDDA
- removed copper zone on In2.Cu, net /STM32WLE5 + Radio/VDDPA
- removed copper zone on In2.Cu, net Net-(IC1-VR_PA)
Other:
- board size 57.8 x 50.1 mm -> 53.5 x 46 mm
